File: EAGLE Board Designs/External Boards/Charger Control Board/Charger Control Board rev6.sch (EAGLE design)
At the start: 114 parts, among them U1 CPC1002N, U2 CDSOT23-T24CAN-Q

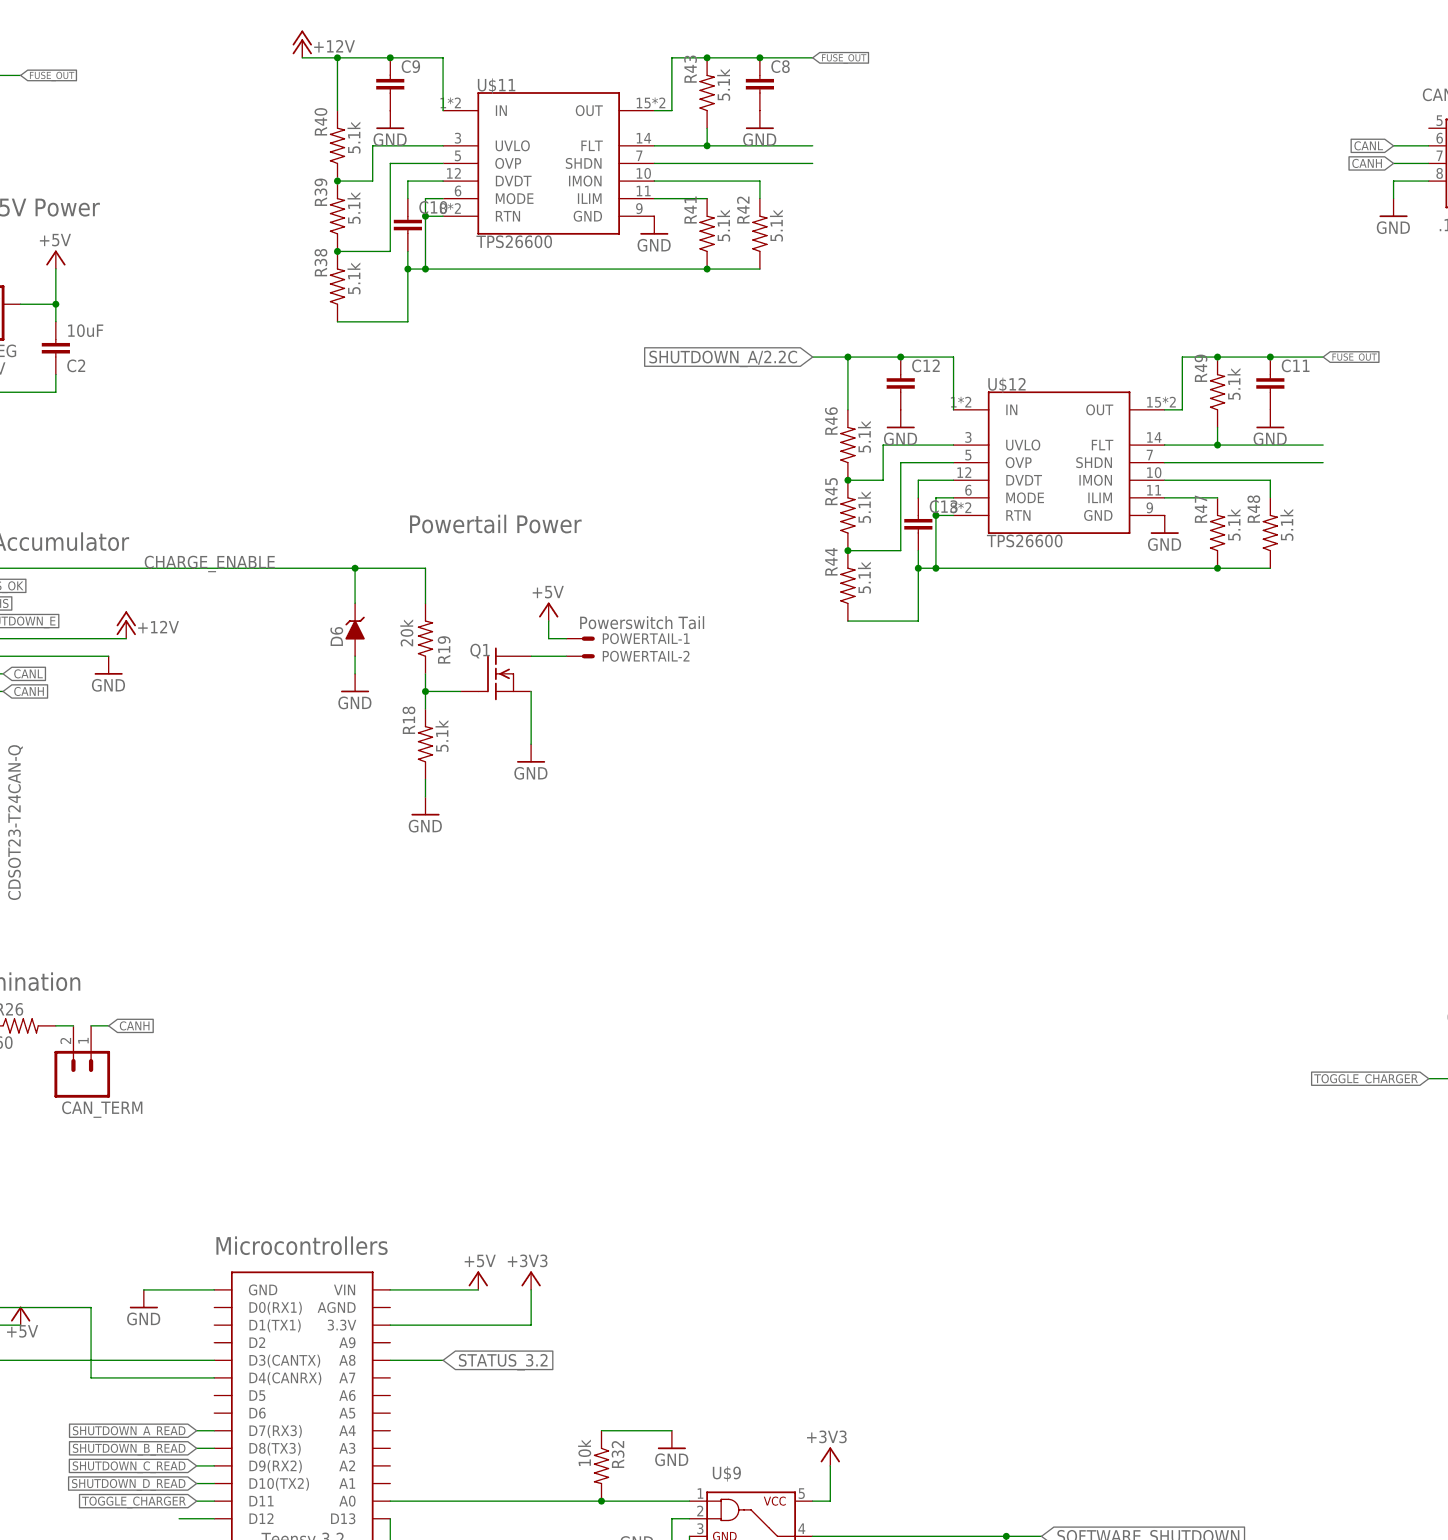
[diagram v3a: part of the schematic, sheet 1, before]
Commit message: Made more changes to implement the e-fuse into the board including adding a current monitoring signal.
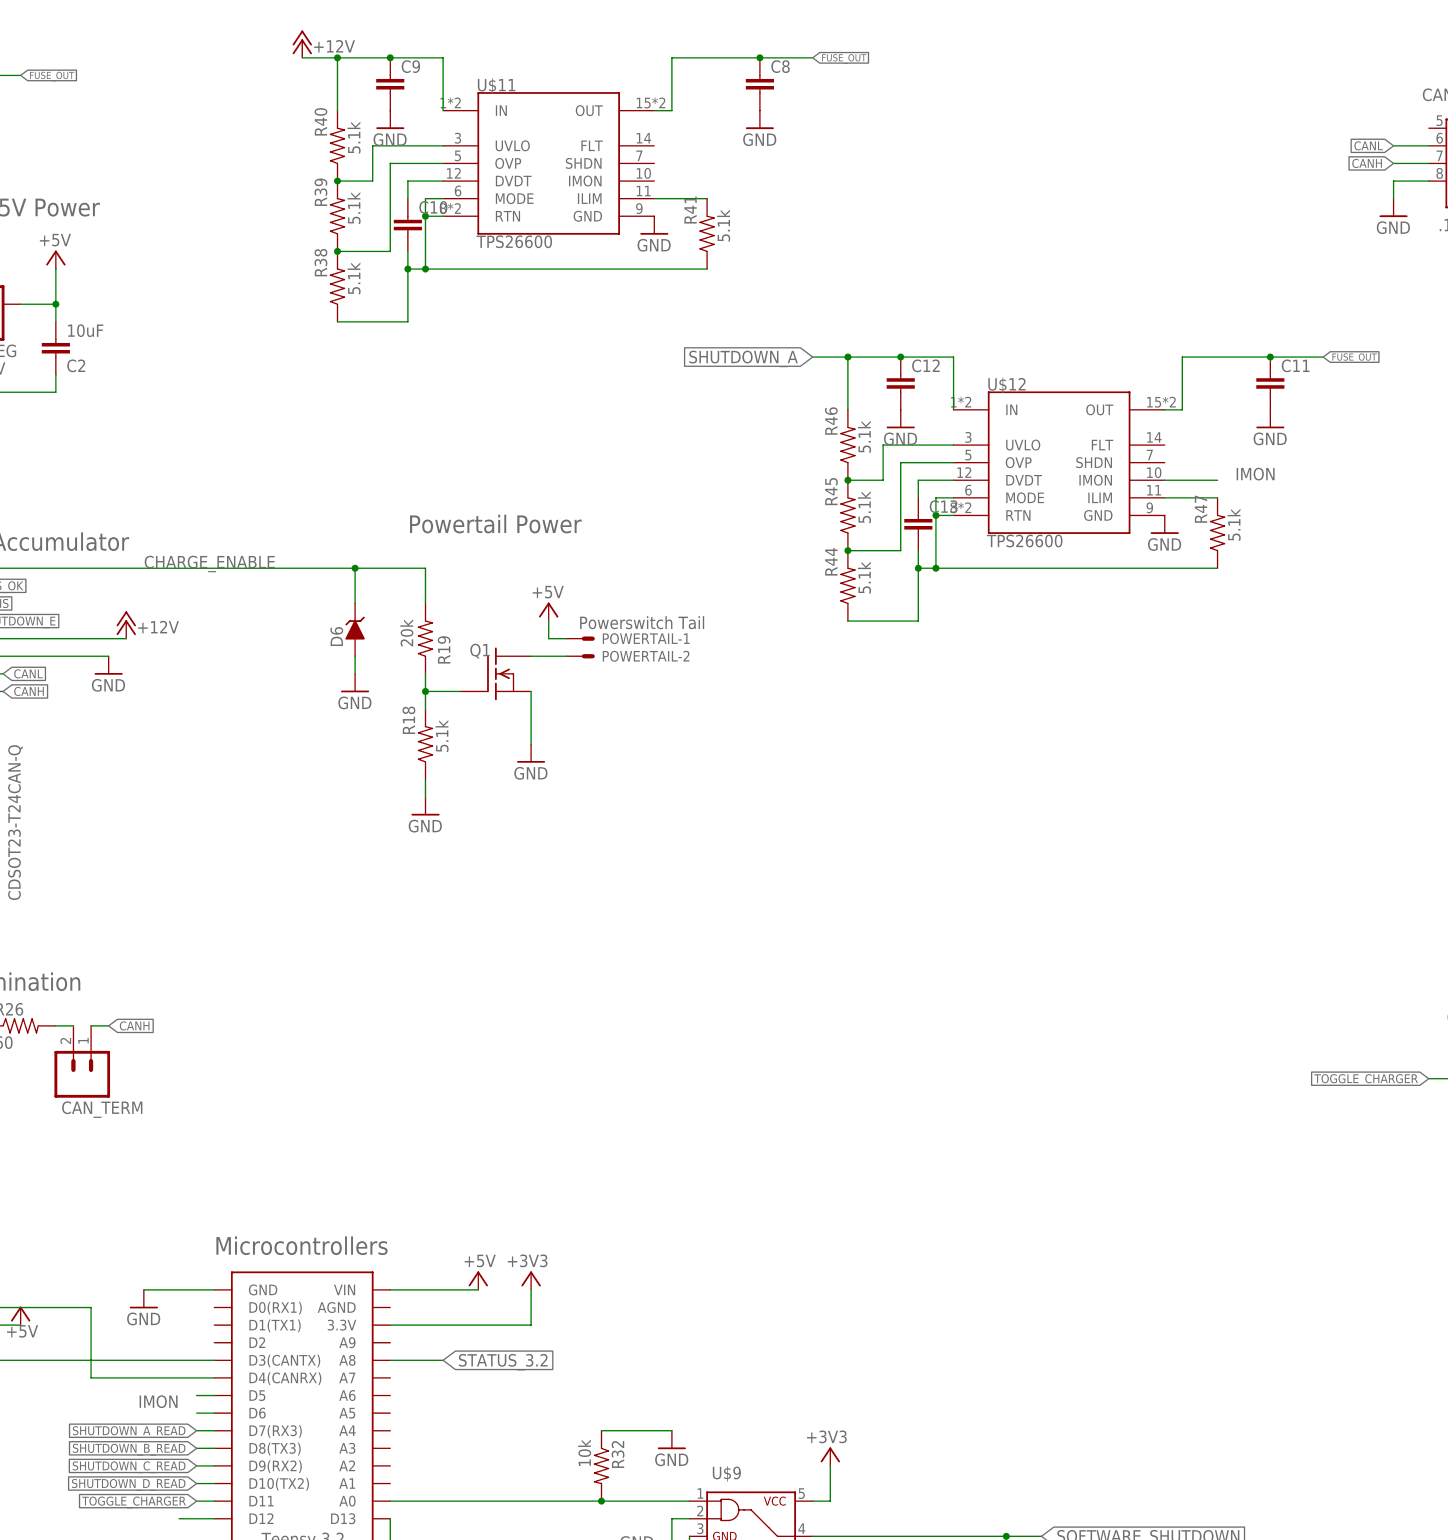
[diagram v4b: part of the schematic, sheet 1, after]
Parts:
- removed R42, R43, R48, R49: 5.1k, HyTechDevices:RESISTOR0603-RES
- C10, C11, C12, C13, C8, C9: device HyTechDevices:CAP0805 -> HyTechDevices:CAP0603-CAP
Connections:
- removed net N$40: R42.2, U$11.IMON
- removed net N$43: U$11.SHDN
- removed net N$47: R48.2, U$12.IMON
- removed net N$48: U$12.SHDN
- removed net N$49: R49.1, U$12.FLT
- removed net SHUTDOWN_A/2.2C: C12.1, R46.2, U$12.IN
- new net IMON: U$12.IMON, U$4.D6
- net FUSE_OUT: no longer R43.2, R49.2
- net N$35: no longer R42.1
- net N$39: no longer R48.1
- net N$42: now also U$4.D5; no longer R43.1, U$11.FLT
- net SHUTDOWN_A: now also C12.1, R46.2, U$12.IN
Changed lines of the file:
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@@
 <attribute name="TOLERANCE" value="1%"/>
 </part>
-<part name="R42" library="HyTechDevices" deviceset="RESISTOR" device="0603-RES" value="5.1k">
-<attribute name="TOLERANCE" value="1%"/>
-</part>
-<part name="R43" library="HyTechDevices" deviceset="RESISTOR" device="0603-RES" value="5.1k">
-<attribute name="TOLERANCE" value="1%"/>
-</part>
-<part name="C8" library="HyTechDevices" deviceset="CAP" device="0805"/>
+<part name="C8" library="HyTechDevices" deviceset="CAP" device="0603-CAP"/>
 <part name="GND45" library="supply1" deviceset="GND" device=""/>
-<part name="C9" library="HyTechDevices" deviceset="CAP" device="0805"/>
+<part name="C9" library="HyTechDevices" deviceset="CAP" device="0603-CAP"/>
 <part name="GND46" library="supply1" deviceset="GND" device=""/>
-<part name="C10" library="HyTechDevices" deviceset="CAP" device="0805"/>
+<part name="C10" library="HyTechDevices" deviceset="CAP" device="0603-CAP"/>
 <part name="U$12" library="HyTechDevices" deviceset="TPS26600" device=""/>
 <part name="GND44" library="supply1" deviceset="GND" device=""/>
@@
 <attribute name="TOLERANCE" value="1%"/>
 </part>
-<part name="R48" library="HyTechDevices" deviceset="RESISTOR" device="0603-RES" value="5.1k">
-<attribute name="TOLERANCE" value="1%"/>
-</part>
-<part name="R49" library="HyTechDevices" deviceset="RESISTOR" device="0603-RES" value="5.1k">
-<attribute name="TOLERANCE" value="1%"/>
-</part>
-<part name="C11" library="HyTechDevices" deviceset="CAP" device="0805"/>
+<part name="C11" library="HyTechDevices" deviceset="CAP" device="0603-CAP"/>
 <part name="GND47" library="supply1" deviceset="GND" device=""/>
-<part name="C12" library="HyTechDevices" deviceset="CAP" device="0805"/>
+<part name="C12" library="HyTechDevices" deviceset="CAP" device="0603-CAP"/>
 <part name="GND48" library="supply1" deviceset="GND" device=""/>
-<part name="C13" library="HyTechDevices" deviceset="CAP" device="0805"/>
+<part name="C13" library="HyTechDevices" deviceset="CAP" device="0603-CAP"/>
 </parts>
 <sheets>
@@
 <attribute name="TOLERANCE" x="167.64" y="226.06" size="0.127" layer="96" rot="R90" display="off"/>
 </instance>
-<instance part="R42" gate="G$1" x="175.26" y="226.06" smashed="yes" rot="R90">
-<attribute name="NAME" x="173.7614" y="227.33" size="1.778" layer="95" rot="R90"/>
-<attribute name="VALUE" x="178.562" y="224.79" size="1.778" layer="96" rot="R90"/>
-<attribute name="TOLERANCE" x="175.26" y="226.06" size="0.127" layer="96" rot="R90" display="off"/>
-</instance>
-<instance part="R43" gate="G$1" x="167.64" y="246.38" smashed="yes" rot="R90">
-<attribute name="NAME" x="166.1414" y="247.65" size="1.778" layer="95" rot="R90"/>
-<attribute name="VALUE" x="170.942" y="245.11" size="1.778" layer="96" rot="R90"/>
-<attribute name="TOLERANCE" x="167.64" y="246.38" size="0.127" layer="96" rot="R90" display="off"/>
-</instance>
 <instance part="C8" gate="G$1" x="175.26" y="246.38" smashed="yes">
 <attribute name="NAME" x="176.784" y="249.301" size="1.778" layer="95"/>
@@
 <attribute name="VALUE" x="244.602" y="181.61" size="1.778" layer="96" rot="R90"/>
 <attribute name="TOLERANCE" x="241.3" y="182.88" size="0.127" layer="96" rot="R90" display="off"/>
-</instance>
-<instance part="R48" gate="G$1" x="248.92" y="182.88" smashed="yes" rot="R90">
-<attribute name="NAME" x="247.4214" y="184.15" size="1.778" layer="95" rot="R90"/>
-<attribute name="VALUE" x="252.222" y="181.61" size="1.778" layer="96" rot="R90"/>
-<attribute name="TOLERANCE" x="248.92" y="182.88" size="0.127" layer="96" rot="R90" display="off"/>
-</instance>
-<instance part="R49" gate="G$1" x="241.3" y="203.2" smashed="yes" rot="R90">
-<attribute name="NAME" x="239.8014" y="204.47" size="1.778" layer="95" rot="R90"/>
-<attribute name="VALUE" x="244.602" y="201.93" size="1.778" layer="96" rot="R90"/>
-<attribute name="TOLERANCE" x="241.3" y="203.2" size="0.127" layer="96" rot="R90" display="off"/>
 </instance>
 <instance part="C11" gate="G$1" x="248.92" y="203.2" smashed="yes">
@@
 <pinref part="R41" gate="G$1" pin="1"/>
 <wire x1="167.64" y1="220.98" x2="127" y2="220.98" width="0.1524" layer="91"/>
-<pinref part="R42" gate="G$1" pin="1"/>
-<wire x1="175.26" y1="220.98" x2="167.64" y2="220.98" width="0.1524" layer="91"/>
-<junction x="167.64" y="220.98"/>
 <pinref part="R38" gate="G$1" pin="1"/>
 <wire x1="124.46" y1="220.98" x2="124.46" y2="213.36" width="0.1524" layer="91"/>
@@
 <pinref part="U$11" gate="G$1" pin="ILIM"/>
 <wire x1="167.64" y1="231.14" x2="160.02" y2="231.14" width="0.1524" layer="91"/>
-</segment>
-</net>
-<net name="N$40" class="0">
-<segment>
-<pinref part="R42" gate="G$1" pin="2"/>
-<wire x1="175.26" y1="231.14" x2="175.26" y2="233.68" width="0.1524" layer="91"/>
-<pinref part="U$11" gate="G$1" pin="IMON"/>
-<wire x1="175.26" y1="233.68" x2="160.02" y2="233.68" width="0.1524" layer="91"/>
-</segment>
-</net>
-<net name="N$43" class="0">
-<segment>
-<pinref part="U$11" gate="G$1" pin="SHDN"/>
-<wire x1="160.02" y1="236.22" x2="182.88" y2="236.22" width="0.1524" layer="91"/>
-</segment>
-</net>
-<net name="N$42" class="0">
-<segment>
-<pinref part="R43" gate="G$1" pin="1"/>
-<wire x1="167.64" y1="241.3" x2="167.64" y2="238.76" width="0.1524" layer="91"/>
-<pinref part="U$11" gate="G$1" pin="FLT"/>
-<wire x1="167.64" y1="238.76" x2="160.02" y2="238.76" width="0.1524" layer="91"/>
-<junction x="167.64" y="238.76"/>
-<wire x1="167.64" y1="238.76" x2="182.88" y2="238.76" width="0.1524" layer="91"/>
 </segment>
 </net>
@@
 <pinref part="R47" gate="G$1" pin="1"/>
 <wire x1="241.3" y1="177.8" x2="200.66" y2="177.8" width="0.1524" layer="91"/>
-<pinref part="R48" gate="G$1" pin="1"/>
-<wire x1="248.92" y1="177.8" x2="241.3" y2="177.8" width="0.1524" layer="91"/>
-<junction x="241.3" y="177.8"/>
 <pinref part="R44" gate="G$1" pin="1"/>
 <wire x1="198.12" y1="177.8" x2="198.12" y2="170.18" width="0.1524" layer="91"/>
@@
 </segment>
 </net>
-<net name="N$47" class="0">
-<segment>
-<pinref part="R48" gate="G$1" pin="2"/>
-<wire x1="248.92" y1="187.96" x2="248.92" y2="190.5" width="0.1524" layer="91"/>
-<pinref part="U$12" gate="G$1" pin="IMON"/>
-<wire x1="248.92" y1="190.5" x2="233.68" y2="190.5" width="0.1524" layer="91"/>
-</segment>
-</net>
-<net name="N$48" class="0">
-<segment>
-<pinref part="U$12" gate="G$1" pin="SHDN"/>
-<wire x1="233.68" y1="193.04" x2="256.54" y2="193.04" width="0.1524" layer="91"/>
-</segment>
-</net>
-<net name="N$49" class="0">
-<segment>
-<pinref part="R49" gate="G$1" pin="1"/>
-<wire x1="241.3" y1="198.12" x2="241.3" y2="195.58" width="0.1524" layer="91"/>
-<pinref part="U$12" gate="G$1" pin="FLT"/>
-<wire x1="241.3" y1="195.58" x2="233.68" y2="195.58" width="0.1524" layer="91"/>
-<junction x="241.3" y="195.58"/>
-<wire x1="241.3" y1="195.58" x2="256.54" y2="195.58" width="0.1524" layer="91"/>
-</segment>
-</net>
 <net name="N$50" class="0">
 <segment>
@@
 </segment>
 </net>
-<net name="SHUTDOWN_A/2.2C" class="0">
+<net name="SHUTDOWN_A" class="0">
 <segment>
 <pinref part="U$12" gate="G$1" pin="IN"/>
@@
 <wire x1="160.02" y1="243.84" x2="162.56" y2="243.84" width="0.1524" layer="91"/>
 <wire x1="162.56" y1="243.84" x2="162.56" y2="251.46" width="0.1524" layer="91"/>
-<pinref part="R43" gate="G$1" pin="2"/>
-<wire x1="162.56" y1="251.46" x2="167.64" y2="251.46" width="0.1524" layer="91"/>
-<wire x1="167.64" y1="251.46" x2="175.26" y2="251.46" width="0.1524" layer="91"/>
-<junction x="167.64" y="251.46"/>
+<wire x1="162.56" y1="251.46" x2="175.26" y2="251.46" width="0.1524" layer="91"/>
 <pinref part="C8" gate="G$1" pin="1"/>
 <wire x1="175.26" y1="251.46" x2="182.88" y2="251.46" width="0.1524" layer="91"/>
@@
 <wire x1="233.68" y1="200.66" x2="236.22" y2="200.66" width="0.1524" layer="91"/>
 <wire x1="236.22" y1="200.66" x2="236.22" y2="208.28" width="0.1524" layer="91"/>
-<pinref part="R49" gate="G$1" pin="2"/>
-<wire x1="236.22" y1="208.28" x2="241.3" y2="208.28" width="0.1524" layer="91"/>
-<wire x1="241.3" y1="208.28" x2="248.92" y2="208.28" width="0.1524" layer="91"/>
-<junction x="241.3" y="208.28"/>
+<wire x1="236.22" y1="208.28" x2="248.92" y2="208.28" width="0.1524" layer="91"/>
 <pinref part="C11" gate="G$1" pin="1"/>
 <wire x1="248.92" y1="208.28" x2="256.54" y2="208.28" width="0.1524" layer="91"/>
@@
 </segment>
 </net>
+<net name="IMON" class="0">
+<segment>
+<pinref part="U$12" gate="G$1" pin="IMON"/>
+<wire x1="233.68" y1="190.5" x2="241.3" y2="190.5" width="0.1524" layer="91"/>
+<label x="243.84" y="190.5" size="1.778" layer="95"/>
+</segment>
+<segment>
+<pinref part="U$4" gate="G$1" pin="D6"/>
+<wire x1="96.52" y1="55.88" x2="93.98" y2="55.88" width="0.1524" layer="91"/>
+<label x="91.44" y="58.42" size="1.778" layer="95" rot="R180"/>
+</segment>
+</net>
+<net name="N$42" class="0">
+<segment>
+<pinref part="U$4" gate="G$1" pin="D5"/>
+<wire x1="93.98" y1="58.42" x2="96.52" y2="58.42" width="0.1524" layer="91"/>
+</segment>
+</net>
